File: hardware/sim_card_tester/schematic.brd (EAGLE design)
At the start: 160 x 100 mm, 139 parts, among them IC1 TPS6300, J13 U.FL-R-SMT, J2 MICRO_USB_B_HIROSE_ZX62R-B-5P, J3 CON_MICRO_SDDM3AT-SF-PEJM5, J4 NANO_SIM, J5 NANO_SIM, J6 TC2030-JLINK-NL, J7 NANO_SIM, J8 NANO_SIM, Q1 MOSFET-NCHANNELSMD, Q2 MOSFET-NCHANNELSMD, Q6 MOSFET-NCHANNELSMD, Q7 SI223DDS, U1 AB1815-T3, U10 SIP32510, U11 SIP32510, U12 UBLOX_SARA_G350, U13 TXB0104RUT, U15 MAX4734EUB+, U2 BGA725L6-ALT, U20 MAX4734EUB+, U21 MAX4734EUB+, U22 MAX4734EUB+, U3 FTDI234XD, U4 SAFFB1G56KB0F0A, U5 MAX8887EZK33+T, U6 MCP73831, U7 MAX-M8, U8 MAX67XXMAX6749MAX67XX, U9 NRF52840, X1 ABS07-32.768KHZ-7-T, X4 32MHz, X5 32.768kHz

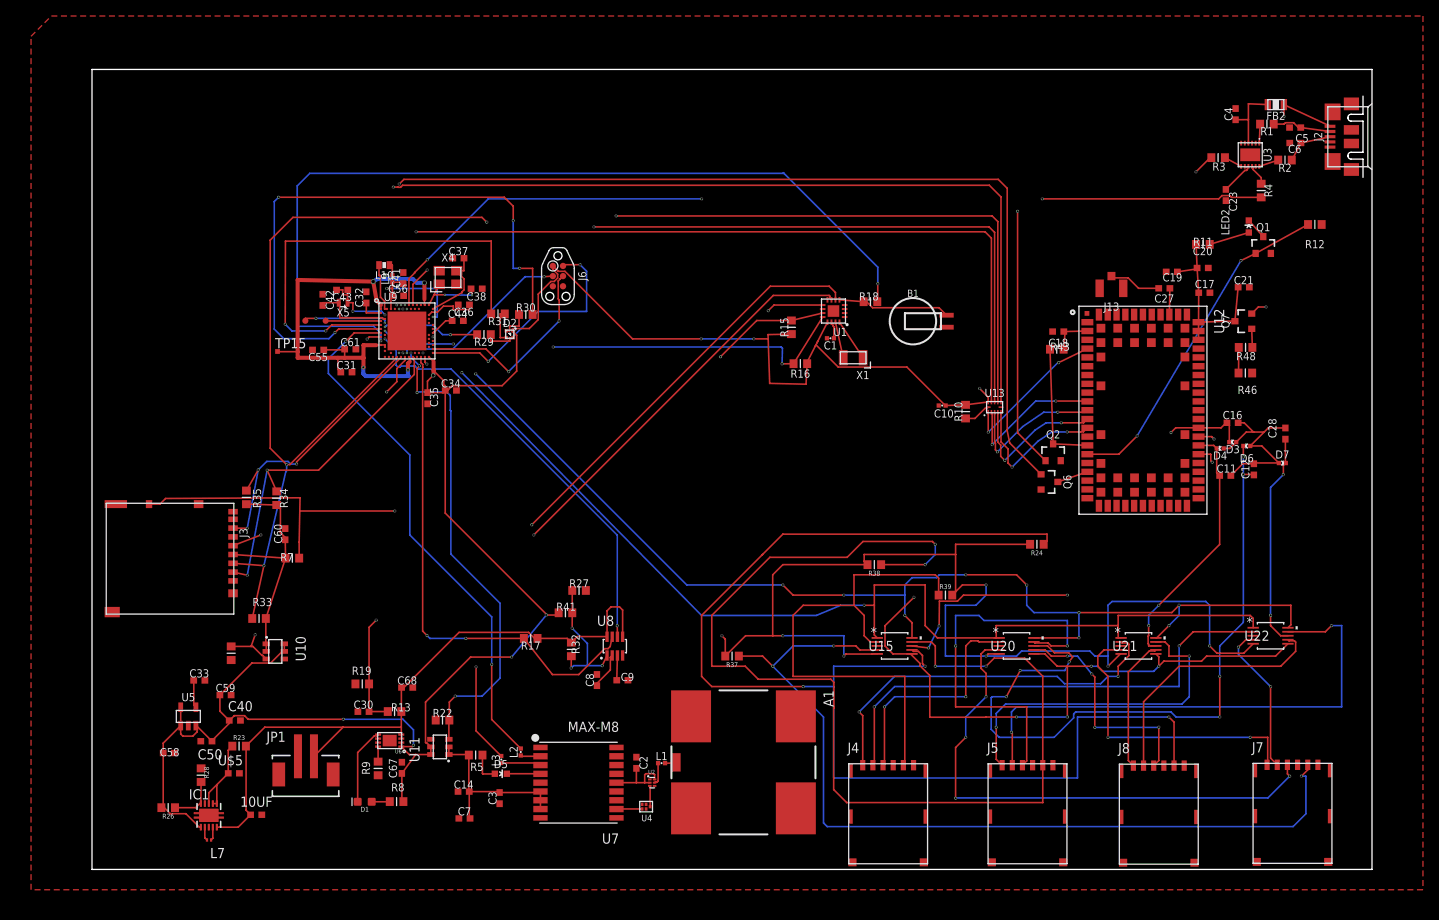
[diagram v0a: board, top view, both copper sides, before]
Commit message: fixed drc errors
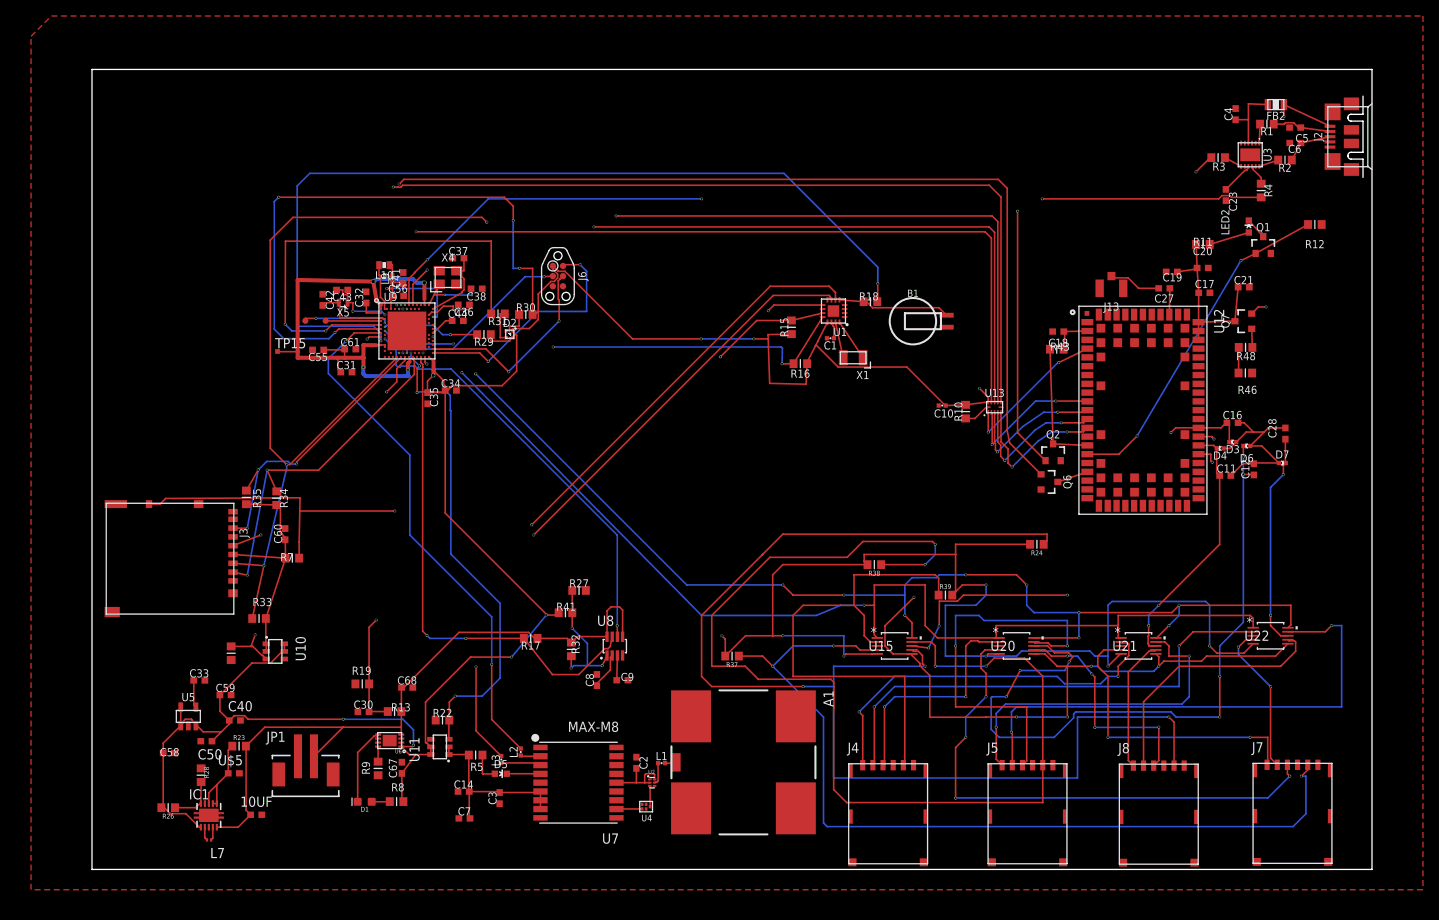
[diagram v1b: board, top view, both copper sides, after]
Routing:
- net +3V3: track 372.8 -> 371.8 mm

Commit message: add ground vias, label parts, clean up board
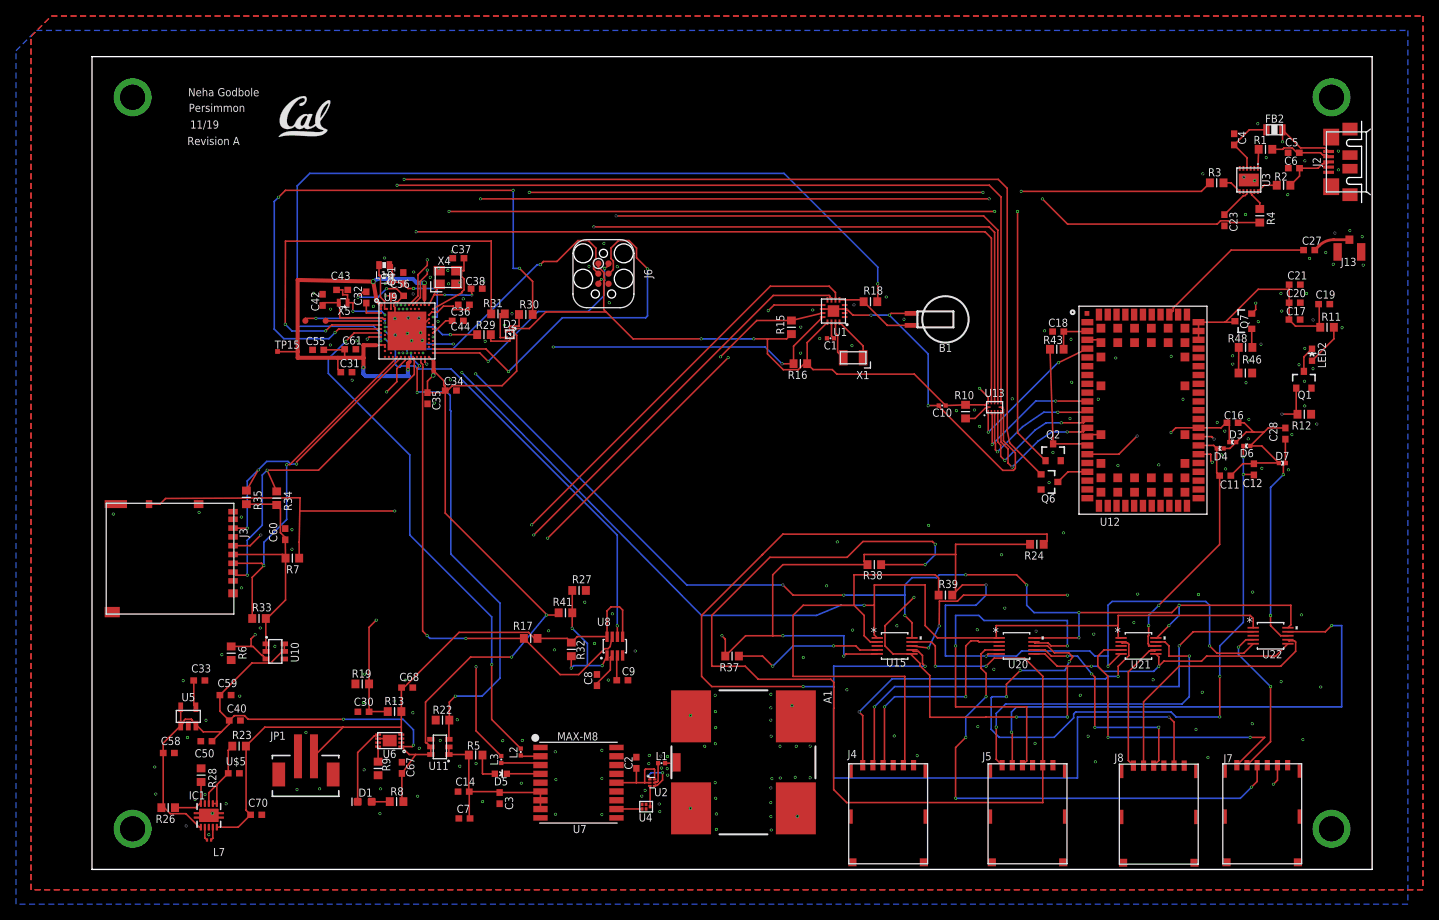
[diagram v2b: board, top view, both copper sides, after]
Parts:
- added U$3: (no value), logos:UCB_CAL_200MIL
- J6: value TC2030-JLINK-NL -> TC2030-JLINK-L; device connector:TC2030-IDC-NL -> connector:TC2030-IDC
- moved J13 30.1 mm to (157.2, 77.2)
- moved R12 23.8 mm to (151.5, 56.9)
- moved C19 19.5 mm to (154.0, 70.7), turned to 0 degrees
- moved C27 18.7 mm to (152.1, 77.4), turned to 0 degrees
- moved R11 18.7 mm to (154.4, 67.8)
- moved LED2 17.9 mm to (152.5, 64.3)
- moved Q1 17.6 mm to (151.5, 61.2)
- moved C20 12.3 mm to (150.3, 70.8)
- moved C17 11.8 mm to (150.3, 68.7)
- moved C21 6.38 mm to (150.3, 73.1)
- moved J6 5.70 mm to (63.9, 74.5)
- moved B1 4.07 mm to (106.7, 68.8), turned to 180 degrees
- moved J7 3.78 mm to (146.3, 6.96)
- moved C6 3.15 mm to (150.2, 87.7)
- moved R2 3.15 mm to (148.9, 85.5)
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- renumbered 10UF to C70
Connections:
- net GND: now also U1.10
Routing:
- net GND: track 0.25 -> 76.5 mm, vias 0 -> 239
- net NRF_SWDCLK: track 25.5 -> 47.6 mm
- net NRF_MOSI: track 147.3 -> 127.9 mm, vias 4 -> 5
- net N$69: track 3.29 -> 20.3 mm
- net !NRF_RST: track 22.4 -> 33.6 mm
- net GSM_LED: track 42.2 -> 31.7 mm
- net VCC3: track 109.5 -> 101.5 mm
- net +3V3: track 371.8 -> 364.0 mm
- net GSM_GATED: track 23.3 -> 28.2 mm
- net RST3: track 66.8 -> 63.0 mm
- net N$5: track 14.1 -> 10.7 mm
- net VCC: track 166.7 -> 164.1 mm
- net N$70: track 6.54 -> 4.71 mm
- net UART_RX: track 109.2 -> 107.5 mm, vias 2 -> 4
- net UART_TX: track 114.2 -> 115.9 mm, vias 3 -> 4
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- added copper zone on layer 16, net GND
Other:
- board size 160 x 100 mm -> 160 x 101.6 mm
- board text added: "11/19"
- board text added: "Neha Godbole"
- board text added: "Persimmon"
- board text added: "Revision A"

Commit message: renumbered
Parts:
- removed C50, C70: 10uF, Nordic_nRF:RESC0603_L
- removed C55, C56: 1uF, Nordic_nRF:RESC0603_L
- removed C58, C59, C60, C67, C68: 4.7uF, Nordic_nRF:RESC0603_L
- removed J13: U.FL-R-SMT, connector:U.FL_SMT
- removed L7: 2.2u, Nordic_nRF:RESC0201_L
- removed L9: 15nH, passives:0402_CAP
- removed Q6: MOSFET-NCHANNELSMD, fets:SOT23-3
- removed R39: 10k, BeagleBone_Black_Wireless:R0603
- removed R41: 1M, BeagleBone_Black_Wireless:R0603
- removed R43, R46: 100k, BeagleBone_Black_Wireless:R0603
- removed R48: 100, BeagleBone_Black_Wireless:R0603
- added C13: 56pF, Nordic_nRF:RESC0603_L
- added C15: 820pF, Nordic_nRF:RESC0603_L
- added C22, C24, C25, C26: 0.1uF, Nordic_nRF:RESC0603_L
- added C29: 100nF, Nordic_nRF:RESC0603_L
- added C45: 100uF, Nordic_nRF:RESC0603_L
- added C46: 220uF, Nordic_nRF:RESC0603_L
- added J1: CON_MICRO_SDDM3AT-SF-PEJM5, connector:DM3AT-SF-PEJM5
- added L5, L6: 1kH, passives:0402_CAP
- added Q3: MOSFET-NCHANNELSMD, fets:SOT23-3
- added R14, R20, R21, R25: 10k, BeagleBone_Black_Wireless:R0603
- added R36: 1.3M, BeagleBone_Black_Wireless:R0603
- C1: value 47pF -> 12pF; device passives:0402_CAP -> Nordic_nRF:RESC0603_L
- C10: value 1uF -> 47pF; device passives:0402_CAP -> Nordic_nRF:RESC0603_L
- C14: value 10uF -> 100pF
- C16: value 47pF -> 10nF
- C17: value 56pF -> 10nF
- C18: value 100uF -> 10nF
- C2, C3, C4: value 10nF -> 12pF
- C20: value 220uF -> 10nF
- C21: value 100nF -> 47nF
- C23: value 100nF -> 0.1uF
- C27: value 33pF -> 0.1uF
- C28: value 47pF -> 100nF
- C30: value 0.1uF -> 0.82uF
- C31: value 0.1uF -> 1uF; device Nordic_nRF:RESC0603_L -> passives:0402_CAP
- C32: value 0.1uF -> 1uF
- C33: value 10nF -> 1uF
- C34: value 0.1uF -> 2.2uF
- C35: value 0.1uF -> 4.7uF
- C36: value 100pF -> 4.7uF
- C37, C38: value 12pF -> 4.7uF
- C40: value 10uF -> 4.7uF
- C41: value 47nF -> 10uF
- C42, C43: value 12pF -> 10uF
- C44: value 820pF -> 10uF
- C5: value 47pF -> 33pF
- C6: device Nordic_nRF:RESC0603_L -> passives:0402_CAP
- C7: value 0.1uF -> 47pF
- C8: value 2.2uF -> 47pF
- C9: value 0.82uF -> 47pF
- J3: value CON_MICRO_SDDM3AT-SF-PEJM5 -> NANO_SIM; device connector:DM3AT-SF-PEJM5 -> signpost:WURTH_NANO_SIM
- J6: value TC2030-JLINK-L -> NANO_SIM; device connector:TC2030-IDC -> signpost:WURTH_NANO_SIM
- J7: value NANO_SIM -> TC2030-JLINK-L; device signpost:WURTH_NANO_SIM -> connector:TC2030-IDC
- J8: value NANO_SIM -> U.FL-R-SMT; device signpost:WURTH_NANO_SIM -> connector:U.FL_SMT
- L2: value 1k -> 15nH
- L3: value 1k -> 2.2uH; device passives:0402_CAP -> Nordic_nRF:RESC0201_L
- R1, R2: value 27Ω -> 27
- R10: value 10k -> 1k
- R12: value 100k -> 1k
- R13: value 10M -> 2k
- R19: value 2.2M -> 10k
- R22: value 100k -> 10k
- R23: value 100 -> 10k
- R26: value 1.3M -> 100k
- R27: value 499k -> 100k
- R28: value 200k -> 100k
- R29, R30, R31: value 470 -> 100k
- R3, R4: value 100Ω -> 100
- R32: value 825k -> 200k
- R33: value 10k -> 499k
- R34: value 10k -> 825k
- R35: value 10k -> 1M
- R37: value 10k -> 2.2M
- R38: value 10k -> 10M
- R5: value 1k -> 100
- R6: value 100k -> 100
- R7: value 100k -> 470
- R8: value 1k -> 470
- R9: value 2k 1% -> 470
- moved C19 148.3 mm to (13.4, 23.6)
- moved C7 132.9 mm to (150.2, 89.6), turned to 180 degrees
- moved R6 132.4 mm to (144.2, 65.3), turned to 180 degrees
- moved R11 130.5 mm to (38.1, 8.48), turned to 0 degrees
- moved C23 123.9 mm to (33.9, 19.7), turned to 0 degrees
- moved C17 116.0 mm to (51.0, 8.92), turned to 90 degrees
- moved C4 113.1 mm to (31.3, 72.4), turned to 180 degrees
- moved C27 111.8 mm to (41.9, 58.9), turned to 270 degrees
- moved C21 111.4 mm to (38.9, 73.9), turned to 90 degrees
- moved C8 108.1 mm to (150.2, 87.7), turned to 180 degrees
- moved J7 106.5 mm to (63.9, 74.5), turned to 270 degrees
- moved R31 101.6 mm to (151.5, 56.9)
- moved J6 96.9 mm to (133.3, 6.91), turned to 0 degrees
- moved R30 90.2 mm to (144.2, 62.1), turned to 180 degrees
- moved J3 87.9 mm to (99.5, 6.96), turned to 0 degrees
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- renumbered C61 to C39, FB2 to FB1, L10 to L4, LED2 to LED1, Q7 to Q4
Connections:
- net !CHRG: now also R11.1; no longer R8.1
- net !EXTERNAL_RST: now also R16.2; no longer R17.2
- net !NRF_CS_SD: now also J1.2, R19.1; no longer J3.2, R34.1
- net !NRF_RST: now also J7.3; no longer J6.3
- net !RTC_CS: now also R15.2, R17.2; no longer R16.2, R18.2
- net !RTC_INT1: now also R14.2; no longer R15.2
- net !SD_DETECT: now also J1.A, R28.1; no longer J3.A, R7.1
- net +3V3: now also C24.1, C26.1, C27.1, C32.1, C37.1, C38.1, C43.1, C44.1, J7.1, R11.2, R14.1, R25.2, R35.1, R36.2; no longer C10.1, C34.1, C40.1, C50.1, C55.1, C58.1, C59.1, C67.1, J6.1, R10.2, R16.1, R26.2, R41.1, R8.2
- net BAT: now also C36.1, C42.1, R16.1, R34.1, R38.2, R5.2; no longer C68.1, C70.1, R13.2, R17.1, R23.2, R32.1
- net BATIN: now also C23.2, R37.2, R38.1; no longer C30.2, R13.1, R19.2
- net CLK1: now also J3.C3; no longer J4.C3
- net CLK2: now also J4.C3; no longer J5.C3
- net CLK3: now also J5.C3; no longer J7.C3
- net CLK4: now also J6.C3; no longer J8.C3
- net CLK_SIM: now also C12.1; no longer C28.1
- net D+: now also C8.1; no longer C6.1
- net D-: now also C7.1; no longer C5.1
- net GND: now also C1.1, C13.2, C14.2, C15.2, C16.1, C17.1, C22.1, C23.1, C24.2, C25.2, C26.2, C27.2, C28.2, C29.2, C30.2, C37.2, C38.2, C4.1, C41.1, C42.2, C43.2, C45.2, C46.2, C7.2, J1.6, J1.B, J1.MOUNT0, J1.MOUNT1, J1.MOUNT2, J1.MOUNT3, J3.C5, J6.C5, J7.5, J8.GND1, J8.GND2, Q3.2, R13.1, R26.1, R30.1, R31.1, R32.1, R33.2, R37.1; no longer C1.2, C10.2, C14.1, C17.2, C23.2, C30.1, C37.1, C38.1, C4.2, C41.2, C42.1, C43.1, C5.2, C50.2, C55.2, C56.2, C58.2, C59.2, C60.2, C67.2, C68.2, C7.1, C70.2, C9.2, J13.GND1, J13.GND2, J3.6, J3.B, J3.MOUNT0, J3.MOUNT1, J3.MOUNT2, J3.MOUNT3, J6.5, J7.C5, J8.C5, Q6.2, R12.1, R19.1, R22.1, R28.1, R46.1, R6.2, R9.1
- net GPS_PWR_EN: now also R26.2; no longer R22.2
- net GPS_RXD: now also L6.2; no longer L3.2
- net GPS_TXD: now also L5.2; no longer L2.2
- net GPS_VCC: now also C17.2, C22.2, C41.2, R10.2; no longer C14.2, C3.2, C7.2, R5.2
- net GSM_GATED: now also C13.1, C29.1, C46.1, R12.2; no longer C17.1, C19.1, C21.1, R11.2
- net GSM_LED: now also Q3.1, R31.2; no longer Q1.1, R12.2
- net GSM_POWER: now also Q1.1; no longer Q2.1
- net GSM_POWER_GATE: now also R30.2, R6.2; no longer R46.2, R48.2
- net GSM_RST: now also Q2.1; no longer Q6.1
- net IO1: now also J3.C7; no longer J4.C7
- net IO2: now also J4.C7; no longer J5.C7
- net IO3: now also J5.C7; no longer J7.C7
- net IO4: now also J6.C7; no longer J8.C7
- net IO_SIM: now also C9.1; no longer C11.1
- net LED_NRF_BLUE: now also R9.2; no longer R31.2
- net LED_NRF_GREEN: now also R8.2; no longer R30.2
- net LED_NRF_RED: now also R7.2; no longer R29.2
- net MUX_EN: now also R21.2, R22.2, R23.2; no longer R37.2, R38.2, R39.2
- net N$1: now also R10.1; no longer R5.1
- net N$13: now also C6.1; no longer C1.1
- net N$14: now also Q3.3; no longer Q1.3
- net N$15: now also Q2.3; no longer Q6.3
- net N$16: now also C45.1, R29.2; no longer C18.1, R43.2
- net N$17: now also R13.2; no longer R9.2
- net N$18: now also Q1.3, R29.1; no longer Q2.3, R43.1
- net N$22: now also L3.1; no longer L7.1
- net N$23: now also R12.1; no longer R11.1
- net N$26: now also L3.2; no longer L7.2
- net N$27: now also C25.1; no longer C32.1
- net N$28: now also C18.1; no longer C4.1
- net N$29: now also R5.1; no longer R23.1
- net N$31: now also R33.1, R34.2, R35.2; no longer R27.1, R32.2, R41.2
- net N$32: now also C21.1, C33.1, L2.1; no longer C41.1, C56.1, L9.1
- net N$33: now also R32.2, R36.1; no longer R26.1, R28.2
- net N$34: now also C14.1; no longer C36.1
- net N$35: now also C19.1; no longer C33.1
- net N$36: now also C30.1; no longer C9.1
- net N$39: now also C34.1; no longer C8.1
- net N$40: now also L5.1; no longer L2.1
- net N$41: now also L6.1; no longer L3.1
- net N$43: now also C1.2; no longer C37.2
- net N$45: now also C2.2; no longer C38.2
- net N$47: now also L2.2; no longer L9.2
- net N$48: now also C15.1; no longer C44.1
- net N$5: now also R17.1; no longer R18.1
- net N$55: now also C40.1, J1.4, R18.2, R19.2, R20.2, R28.2; no longer C60.1, J3.4, R33.2, R34.2, R35.2, R7.2
- net N$59: now also R7.1; no longer R29.1
- net N$60: now also R8.1; no longer R30.1
- net N$61: now also R9.1; no longer R31.1
- net N$66: now also R6.1; no longer R48.1
- net N$68: now also R25.1; no longer R10.1
- net N$69: now also C5.1; no longer C27.1
- net N$70: now also C5.2, J8.SIG; no longer C27.2, J13.SIG
- net N$71: now also C10.2, C9.2; no longer C16.2, C28.2
- net NRF_MISO: now also J1.7, R20.1; no longer J3.7, R35.1
- net NRF_MOSI: now also J1.3, R18.1; no longer J3.3, R33.1
- net NRF_SCK: now also J1.5; no longer J3.5
- net NRF_SWDCLK: now also J7.4; no longer J6.4
- net NRF_SWDIO: now also J7.2; no longer J6.2
- net RST1: now also J3.C2; no longer J4.C2
- net RST2: now also J4.C2; no longer J5.C2
- net RST3: now also J5.C2; no longer J7.C2
- net RST4: now also J6.C2; no longer J8.C2
- net RST_SIM: now also C10.1; no longer C12.1
- net SD_EN: now also R27.1; no longer R6.1
- net VCC1: now also J3.C1, R24.1; no longer J4.C1, R39.1
- net VCC2: now also J4.C1, R23.1; no longer J5.C1, R38.1
- net VCC3: now also J5.C1, R22.1; no longer J7.C1, R37.1
- net VCC4: now also J6.C1, R21.1; no longer J8.C1, R24.1
- net VCC_LINUX_1V8: now also C28.1; no longer C23.1
- net VCC_RF: now also C16.2; no longer C2.2
- net VCC_SIM: now also C11.1; no longer C16.1
- net XL3: now also C4.2; no longer C43.2
- net XL4: now also C3.2; no longer C42.2

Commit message: fixed some wires
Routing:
- net GPS_RXD: track 62.9 -> 63.5 mm

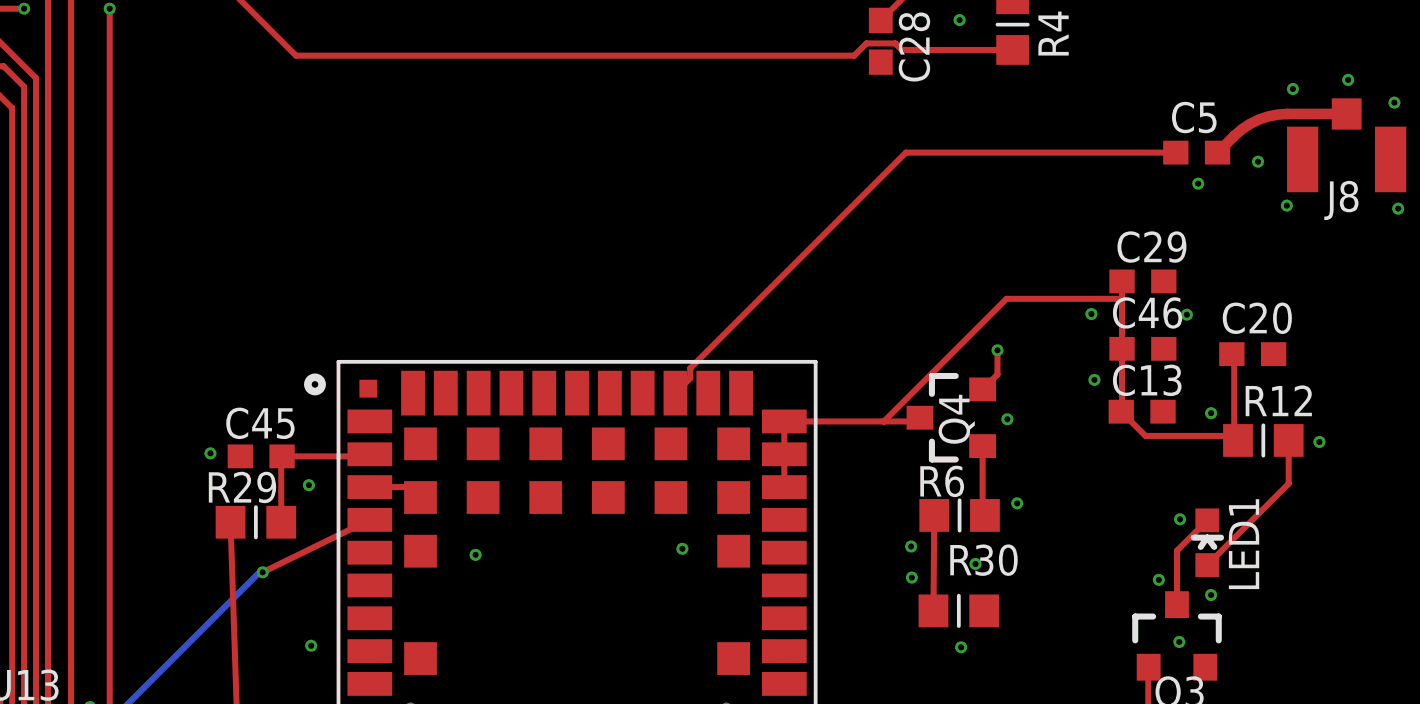
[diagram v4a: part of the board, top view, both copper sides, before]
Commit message: updated parts for caps
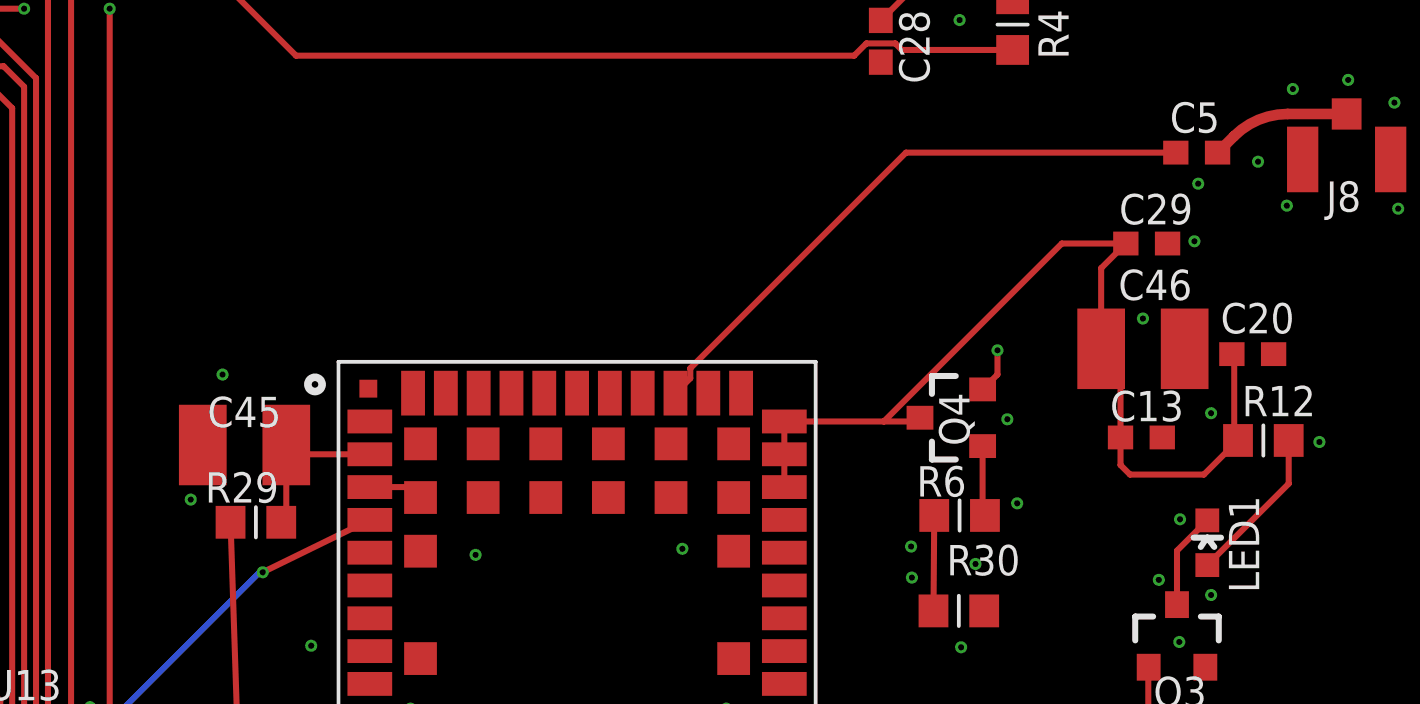
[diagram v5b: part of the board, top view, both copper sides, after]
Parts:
- C45, C46: device Nordic_nRF:RESC0603_L -> BeagleBone_Black_Wireless:C1210
- moved C29 1.28 mm to (150.5, 74.4)
- moved C13 0.86 mm to (150.3, 67.9)
- moved C45 0.68 mm to (120.2, 67.6)
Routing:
- net GSM_GATED: track 28.2 -> 33.2 mm
- net N$16: track 5.38 -> 5.94 mm
- net GND: vias 239 -> 238

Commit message: added most of the parts
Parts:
- L1, L2: device passives:0402_CAP -> Nordic_nRF:RESC0603_M
- L3: device Nordic_nRF:RESC0201_L -> Nordic_nRF:RESC0603_M
- L4: device passives:0603_CAP -> Nordic_nRF:RESC0603_M
- L5, L6: value 1kH -> 1k; device passives:0402_CAP -> Nordic_nRF:RESC0603_M
- moved L2 3.81 mm to (39.6, 77.1), turned to 180 degrees
- moved L5 3.68 mm to (52.7, 18.2)
- moved L6 2.20 mm to (53.3, 14.0)
- moved C20 1.30 mm to (155.3, 70.8)
- moved L4 1.20 mm to (35.5, 76.2), turned to 270 degrees
- moved L1 0.94 mm to (70.5, 13.9)
- moved L3 0.69 mm to (14.6, 3.00)
- moved C16 0.58 mm to (67.5, 13.3)
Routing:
- net N$32: track 15.7 -> 23.4 mm
- net N$7: track 2.51 -> 5.16 mm
- net GPS_TXD: track 66.6 -> 64.3 mm
- net N$8: track 5.01 -> 2.75 mm
- net GPS_RXD: track 63.5 -> 65.3 mm
- net N$47: track 1.63 -> 3.16 mm
- net LNA_IN: track 2.76 -> 3.83 mm
- net N$22: track 1.69 -> 2.53 mm
- net N$26: track 1.71 -> 2.49 mm
- net GSM_GATED: track 33.2 -> 33.8 mm
- net GND: vias 238 -> 242
